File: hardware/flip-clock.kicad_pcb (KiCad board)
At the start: 2 copper layers, 82.5 x 47.8 mm, 19 parts, among them J1 Screw_Terminal_01x02, J2 Conn_01x04, Q1 TCRT5000, U1 WeMos_D1_mini

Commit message: Switched to TMC
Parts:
- Q1: moved to B.Cu
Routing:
- net /Sense: track 14.1 -> 6.58 mm
- net Net-(Q1-Pad4): track 5.37 -> 0.00 mm
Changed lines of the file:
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@@
       (net 29 "/-") (pinfunction "1") (pintype "input"))
-  )
-  (footprint "KiCad:TCRT5000" (layer "F.Cu")
-    (at 105.41 81.28)
-    (descr "TCRT5000")
-    (tags "Transistor")
-    (property "Arrow Part Number" "TCRT5000")
-    (property "Arrow Price/Stock" "https://www.arrow.com/en/products/tcrt5000/vishay")
-    (property "Description" "VISHAY - TCRT5000. - SENSOR, OPTICAL, TRANSISTOR O/P")
-    (property "Height" "6.8")
-    (property "Manufacturer_Name" "Vishay")
-    (property "Manufacturer_Part_Number" "TCRT5000")
-    (property "Mouser Part Number" "782-TCRT5000")
-    (property "Mouser Price/Stock" "https://www.mouser.co.uk/ProductDetail/Vishay-Semiconductors/TCRT5000/?qs=glpcD2KT6uaaYldHGIIt5g%3D%3D")
-    (property "Sheetfile" "flip-clock.kicad_sch")
-    (property "Sheetname" "")
-    (attr through_hole)
-    (fp_text reference "Q1" (at -0.025 -0.045) (layer "F.SilkS")
-      (effects (font (size 1.27 1.27) (thickness 0.254)))
-    )
-    (fp_text value "TCRT5000" (at -0.025 -0.045) (layer "F.SilkS") hide
-      (effects (font (size 1.27 1.27) (thickness 0.254)))
-    )
-    (fp_text user "${REFERENCE}" (at -0.025 -0.045) (layer "F.Fab")
-      (effects (font (size 1.27 1.27) (thickness 0.254)))
-    )
-    (fp_line (start 5.1 2.9) (end 1.5 2.9) (layer "F.SilkS") (width 0.1))
-    (fp_line (start -4 2.9) (end -1.5 2.9) (layer "F.SilkS") (width 0.1))
-    (fp_line (start 5.1 -2.9) (end 1.5 -2.9) (layer "F.SilkS") (width 0.1))
-    (fp_line (start -5.1 -2.9) (end -5.1 1.525) (layer "F.SilkS") (width 0.1))
-    (fp_line (start -5.1 -2.9) (end -1.5 -2.9) (layer "F.SilkS") (width 0.1))
-    (fp_line (start 5.1 -2.9) (end 5.1 2.9) (layer "F.SilkS") (width 0.1))
-    (fp_line (start 6.1 4.7) (end -6.15 4.7) (layer "F.CrtYd") (width 0.1))
-    (fp_line (start -6.15 -4.79) (end 6.1 -4.79) (layer "F.CrtYd") (width 0.1))
-    (fp_line (start 6.1 -4.79) (end 6.1 4.7) (layer "F.CrtYd") (width 0.1))
-    (fp_line (start -6.15 4.7) (end -6.15 -4.79) (layer "F.CrtYd") (width 0.1))
-    (fp_line (start 5.1 -2.9) (end 5.1 2.9) (layer "F.Fab") (width 0.2))
-    (fp_line (start 5.1 2.9) (end -5.1 2.9) (layer "F.Fab") (width 0.2))
-    (fp_line (start -5.1 2.9) (end -5.1 -2.9) (layer "F.Fab") (width 0.2))
-    (fp_line (start -5.1 -2.9) (end 5.1 -2.9) (layer "F.Fab") (width 0.2))
-    (pad "1" thru_hole rect locked (at -2.75 -1.27) (size 1.5 1.5) (drill 1) (layers *.Cu *.Mask)
-      (net 28 "/Sense") (pinfunction "C") (pintype "passive"))
-    (pad "2" thru_hole circle locked (at -2.75 1.27) (size 1.5 1.5) (drill 1) (layers *.Cu *.Mask)
-      (net 29 "/-") (pinfunction "E") (pintype "passive"))
-    (pad "3" thru_hole circle locked (at 2.75 1.27) (size 1.5 1.5) (drill 1) (layers *.Cu *.Mask)
-      (net 29 "/-") (pinfunction "K") (pintype "passive"))
-    (pad "4" thru_hole circle locked (at 2.75 -1.27) (size 1.5 1.5) (drill 1) (layers *.Cu *.Mask)
-      (net 30 "Net-(Q1-Pad4)") (pinfunction "A") (pintype "passive"))
-    (pad "MH1" np_thru_hole circle locked (at -4.65 2.45) (size 1 1) (drill 1) (layers *.Cu *.Mask))
-    (pad "MH2" np_thru_hole circle locked (at 0 2.45) (size 2.5 2.5) (drill 2.5) (layers *.Cu *.Mask))
-    (pad "MH3" np_thru_hole circle locked (at 0 -2.54) (size 2.5 2.5) (drill 2.5) (layers *.Cu *.Mask))
-    (model "${KIPRJMOD}/LIB_TCRT5000/TCRT5000/3D/TCRT5000.stp"
-      (offset (xyz -5.08 -2.9 -5.08))
-      (scale (xyz 1 1 1))
-      (rotate (xyz 0 0 0))
-    )
   )
   (footprint "Resistor_SMD:R_0805_2012Metric" (layer "F.Cu")
@@
     (pad "1" thru_hole oval locked (at 0 0 180) (size 6 8) (drill oval 3.2 5.2) (layers *.Cu *.Mask)
       (net 11 "GND") (pinfunction "1") (pintype "input"))
+  )
+  (footprint "KiCad:TCRT5000" (layer "B.Cu")
+    (at 105.41 81.28)
+    (descr "TCRT5000")
+    (tags "Transistor")
+    (property "Arrow Part Number" "TCRT5000")
+    (property "Arrow Price/Stock" "https://www.arrow.com/en/products/tcrt5000/vishay")
+    (property "Description" "VISHAY - TCRT5000. - SENSOR, OPTICAL, TRANSISTOR O/P")
+    (property "Height" "6.8")
+    (property "Manufacturer_Name" "Vishay")
+    (property "Manufacturer_Part_Number" "TCRT5000")
+    (property "Mouser Part Number" "782-TCRT5000")
+    (property "Mouser Price/Stock" "https://www.mouser.co.uk/ProductDetail/Vishay-Semiconductors/TCRT5000/?qs=glpcD2KT6uaaYldHGIIt5g%3D%3D")
+    (property "Sheetfile" "flip-clock.kicad_sch")
+    (property "Sheetname" "")
+    (attr through_hole)
+    (fp_text reference "Q1" (at -0.025 0.045) (layer "B.SilkS")
+      (effects (font (size 1.27 1.27) (thickness 0.254)) (justify mirror))
+    )
+    (fp_text value "TCRT5000" (at -0.025 0.045) (layer "B.SilkS") hide
+      (effects (font (size 1.27 1.27) (thickness 0.254)) (justify mirror))
+    )
+    (fp_text user "${REFERENCE}" (at -0.025 0.045) (layer "B.Fab")
+      (effects (font (size 1.27 1.27) (thickness 0.254)) (justify mirror))
+    )
+    (fp_line (start 5.1 -2.9) (end 1.5 -2.9) (layer "B.SilkS") (width 0.1))
+    (fp_line (start -4 -2.9) (end -1.5 -2.9) (layer "B.SilkS") (width 0.1))
+    (fp_line (start 5.1 2.9) (end 1.5 2.9) (layer "B.SilkS") (width 0.1))
+    (fp_line (start -5.1 2.9) (end -5.1 -1.525) (layer "B.SilkS") (width 0.1))
+    (fp_line (start -5.1 2.9) (end -1.5 2.9) (layer "B.SilkS") (width 0.1))
+    (fp_line (start 5.1 2.9) (end 5.1 -2.9) (layer "B.SilkS") (width 0.1))
+    (fp_line (start 6.1 -4.7) (end -6.15 -4.7) (layer "B.CrtYd") (width 0.1))
+    (fp_line (start -6.15 4.79) (end 6.1 4.79) (layer "B.CrtYd") (width 0.1))
+    (fp_line (start 6.1 4.79) (end 6.1 -4.7) (layer "B.CrtYd") (width 0.1))
+    (fp_line (start -6.15 -4.7) (end -6.15 4.79) (layer "B.CrtYd") (width 0.1))
+    (fp_line (start 5.1 2.9) (end 5.1 -2.9) (layer "B.Fab") (width 0.2))
+    (fp_line (start 5.1 -2.9) (end -5.1 -2.9) (layer "B.Fab") (width 0.2))
+    (fp_line (start -5.1 -2.9) (end -5.1 2.9) (layer "B.Fab") (width 0.2))
+    (fp_line (start -5.1 2.9) (end 5.1 2.9) (layer "B.Fab") (width 0.2))
+    (pad "1" thru_hole rect locked (at -2.75 1.27) (size 1.5 1.5) (drill 1) (layers *.Cu *.Mask)
+      (net 28 "/Sense") (pinfunction "C"))
+    (pad "2" thru_hole circle locked (at -2.75 -1.27) (size 1.5 1.5) (drill 1) (layers *.Cu *.Mask)
+      (net 29 "/-") (pinfunction "E"))
+    (pad "3" thru_hole circle locked (at 2.75 -1.27) (size 1.5 1.5) (drill 1) (layers *.Cu *.Mask)
+      (net 29 "/-") (pinfunction "K"))
+    (pad "4" thru_hole circle locked (at 2.75 1.27) (size 1.5 1.5) (drill 1) (layers *.Cu *.Mask)
+      (net 30 "Net-(Q1-Pad4)") (pinfunction "A"))
+    (pad "MH1" np_thru_hole circle locked (at -4.65 -2.45) (size 1 1) (drill 1) (layers *.Cu *.Mask))
+    (pad "MH2" np_thru_hole circle locked (at 0 -2.45) (size 2.5 2.5) (drill 2.5) (layers *.Cu *.Mask))
+    (pad "MH3" np_thru_hole circle locked (at 0 2.54) (size 2.5 2.5) (drill 2.5) (layers *.Cu *.Mask))
+    (model "${KIPRJMOD}/LIB_TCRT5000/TCRT5000/3D/TCRT5000.stp"
+      (offset (xyz -5.08 -2.9 -5.08))
+      (scale (xyz 1 1 1))
+      (rotate (xyz 180 180 180))
+    )
   )
   (footprint "MountingHole:MountingHole_3.2mm_M3_Pad" (layer "B.Cu")
@@
   (segment (start 105.41 74.93) (end 107.0375 74.93) (width 0.25) (layer "F.Cu") (net 27))
   (segment (start 101.2425 74.93) (end 105.41 74.93) (width 0.25) (layer "F.Cu") (net 27))
-  (segment (start 100.838 80.01) (end 99.4175 78.5895) (width 0.25) (layer "F.Cu") (net 28))
   (segment (start 101.6 69.85) (end 101.6 72.136) (width 0.25) (layer "F.Cu") (net 28))
-  (segment (start 102.66 80.01) (end 100.838 80.01) (width 0.25) (layer "F.Cu") (net 28))
   (segment (start 100.584 73.152) (end 99.568 73.152) (width 0.25) (layer "F.Cu") (net 28))
   (segment (start 99.4175 73.3025) (end 99.4175 74.93) (width 0.25) (layer "F.Cu") (net 28))
   (segment (start 99.568 73.152) (end 99.4175 73.3025) (width 0.25) (layer "F.Cu") (net 28))
   (segment (start 101.6 72.136) (end 100.584 73.152) (width 0.25) (layer "F.Cu") (net 28))
-  (segment (start 99.4175 78.5895) (end 99.4175 74.93) (width 0.25) (layer "F.Cu") (net 28))
-  (segment (start 108.8625 77.0655) (end 108.8625 74.93) (width 0.25) (layer "F.Cu") (net 30))
-  (segment (start 108.16 77.768) (end 108.8625 77.0655) (width 0.25) (layer "F.Cu") (net 30))
-  (segment (start 108.16 80.01) (end 108.16 77.768) (width 0.25) (layer "F.Cu") (net 30))
   (zone locked (net 11) (net_name "GND") (layers F&B.Cu) (hatch edge 0.508)
     (connect_pads (clearance 0.508))
@@
     )
   )
-  (zone (net 29) (net_name "/-") (layer "F.Cu") (hatch edge 0.508)
+  (zone locked (net 29) (net_name "/-") (layer "F.Cu") (hatch edge 0.508)
     (connect_pads (clearance 0.254))
     (min_thickness 0.254) (filled_areas_thickness no)
@@
     )
   )
-  (zone (net 0) (net_name "") (layers F&B.Cu) (name "Iso") (hatch edge 0.508)
+  (zone locked (net 0) (net_name "") (layers F&B.Cu) (name "Iso") (hatch edge 0.508)
     (connect_pads (clearance 0))
     (min_thickness 0.254)

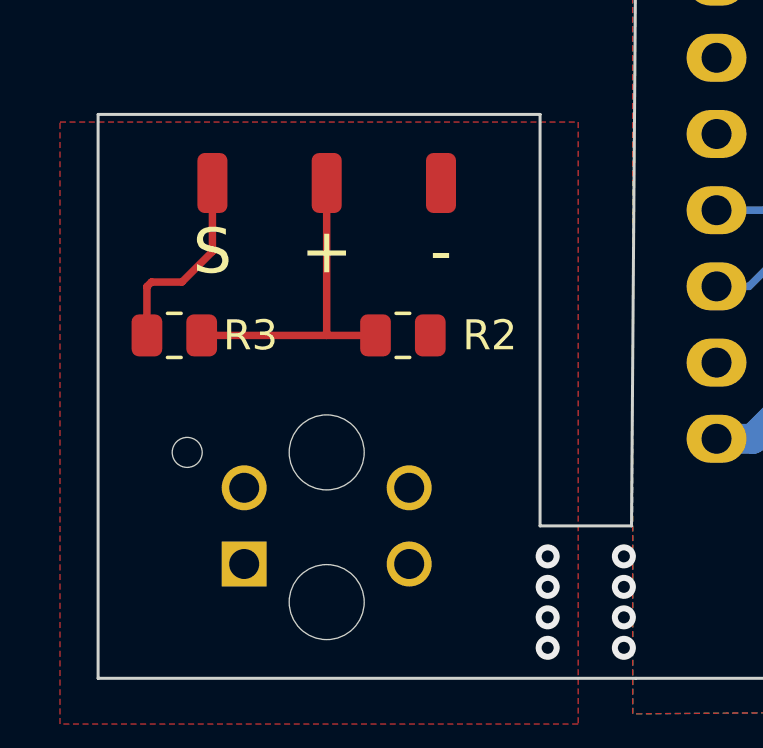
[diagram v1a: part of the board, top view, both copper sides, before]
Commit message: Missing net for flipped IR sensor
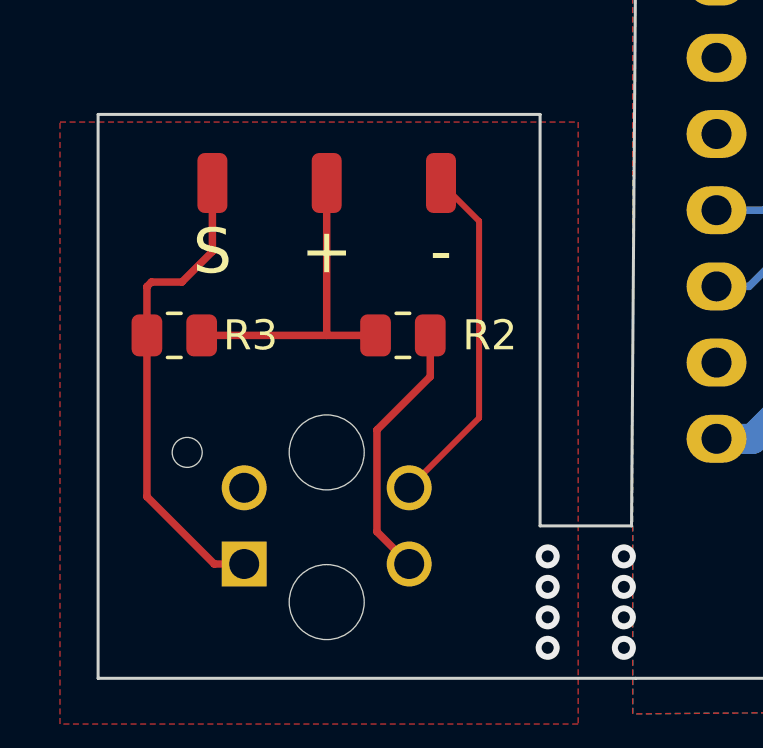
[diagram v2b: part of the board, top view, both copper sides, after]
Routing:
- net /-: track 0.00 -> 11.7 mm
- net /Sense: track 6.58 -> 16.1 mm
- net Net-(Q1-Pad4): track 0.00 -> 8.80 mm
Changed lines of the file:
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@@
   (segment (start 100.584 73.152) (end 99.568 73.152) (width 0.25) (layer "F.Cu") (net 28))
   (segment (start 99.4175 73.3025) (end 99.4175 74.93) (width 0.25) (layer "F.Cu") (net 28))
+  (segment (start 101.66 82.55) (end 99.4175 80.3075) (width 0.25) (layer "F.Cu") (net 28))
   (segment (start 99.568 73.152) (end 99.4175 73.3025) (width 0.25) (layer "F.Cu") (net 28))
   (segment (start 101.6 72.136) (end 100.584 73.152) (width 0.25) (layer "F.Cu") (net 28))
+  (segment (start 99.4175 80.3075) (end 99.4175 74.93) (width 0.25) (layer "F.Cu") (net 28))
+  (segment (start 102.66 82.55) (end 101.66 82.55) (width 0.25) (layer "F.Cu") (net 28))
+  (segment (start 110.49 77.68) (end 108.16 80.01) (width 0.2) (layer "F.Cu") (net 29))
+  (segment (start 109.22 69.85) (end 110.49 71.12) (width 0.2) (layer "F.Cu") (net 29))
+  (segment (start 110.49 71.12) (end 110.49 77.68) (width 0.2) (layer "F.Cu") (net 29))
+  (segment (start 107.085489 78.080511) (end 108.8625 76.3035) (width 0.25) (layer "F.Cu") (net 30))
+  (segment (start 107.085489 81.475489) (end 107.085489 78.080511) (width 0.25) (layer "F.Cu") (net 30))
+  (segment (start 108.16 82.55) (end 107.085489 81.475489) (width 0.25) (layer "F.Cu") (net 30))
+  (segment (start 108.8625 76.3035) (end 108.8625 74.93) (width 0.25) (layer "F.Cu") (net 30))
   (zone locked (net 11) (net_name "GND") (layers F&B.Cu) (hatch edge 0.508)
     (connect_pads (clearance 0.508))
